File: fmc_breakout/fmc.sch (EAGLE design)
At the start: 1 part

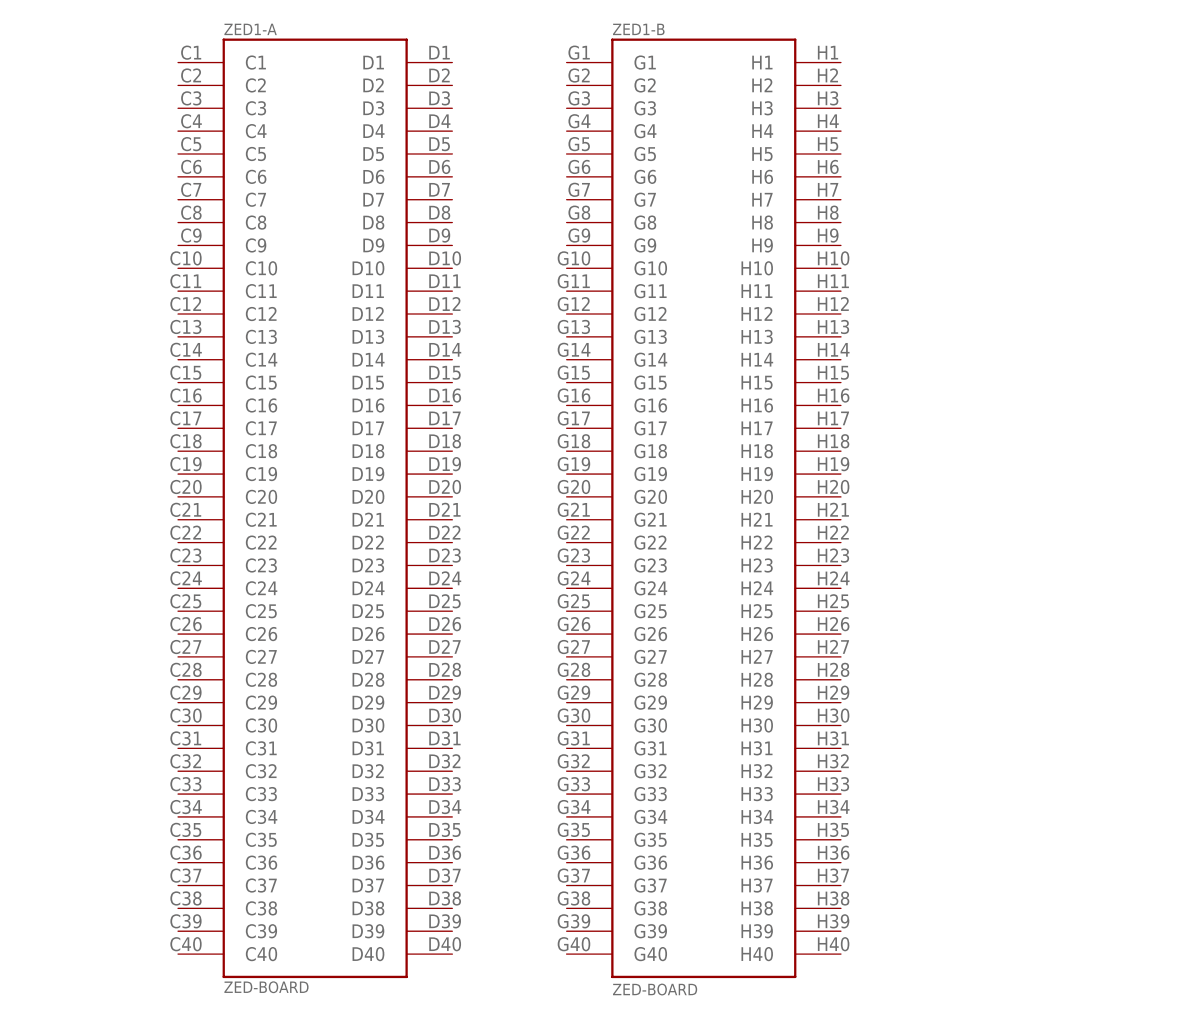
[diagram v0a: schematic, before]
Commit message: started FMC breakout
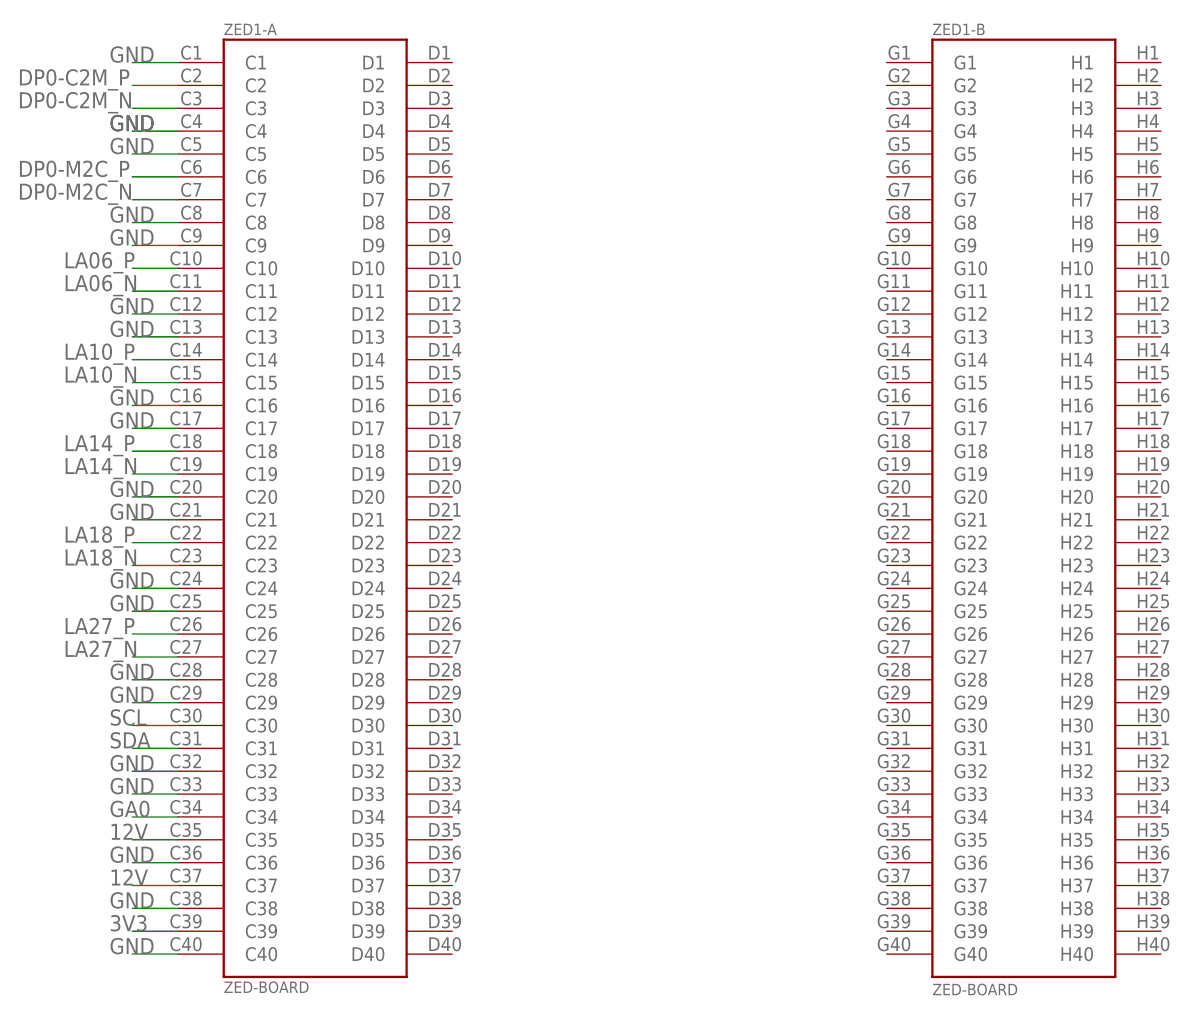
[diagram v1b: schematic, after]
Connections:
- new net 12V: ZED1-A.C35, ZED1-A.C37
- new net 3V3: ZED1-A.C39
- new net DP0-C2M_N: ZED1-A.C3
- new net DP0-C2M_P: ZED1-A.C2
- new net DP0-M2C_N: ZED1-A.C7
- new net DP0-M2C_P: ZED1-A.C6
- new net GA0: ZED1-A.C34
- new net GND: ZED1-A.C1, ZED1-A.C12, ZED1-A.C13, ZED1-A.C16, ZED1-A.C17, ZED1-A.C20, ZED1-A.C21, ZED1-A.C24, ZED1-A.C25, ZED1-A.C28, ZED1-A.C29, ZED1-A.C32, ZED1-A.C33, ZED1-A.C36, ZED1-A.C38, ZED1-A.C4, ZED1-A.C40, ZED1-A.C5, ZED1-A.C8, ZED1-A.C9
- new net LA06_N: ZED1-A.C11
- new net LA06_P: ZED1-A.C10
- new net LA10_N: ZED1-A.C15
- new net LA10_P: ZED1-A.C14
- new net LA14_N: ZED1-A.C19
- new net LA14_P: ZED1-A.C18
- new net LA18_N: ZED1-A.C23
- new net LA18_P: ZED1-A.C22
- new net LA27_N: ZED1-A.C27
- new net LA27_P: ZED1-A.C26
- new net SCL: ZED1-A.C30
- new net SDA: ZED1-A.C31
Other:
- moved on the sheet: ZED1-B

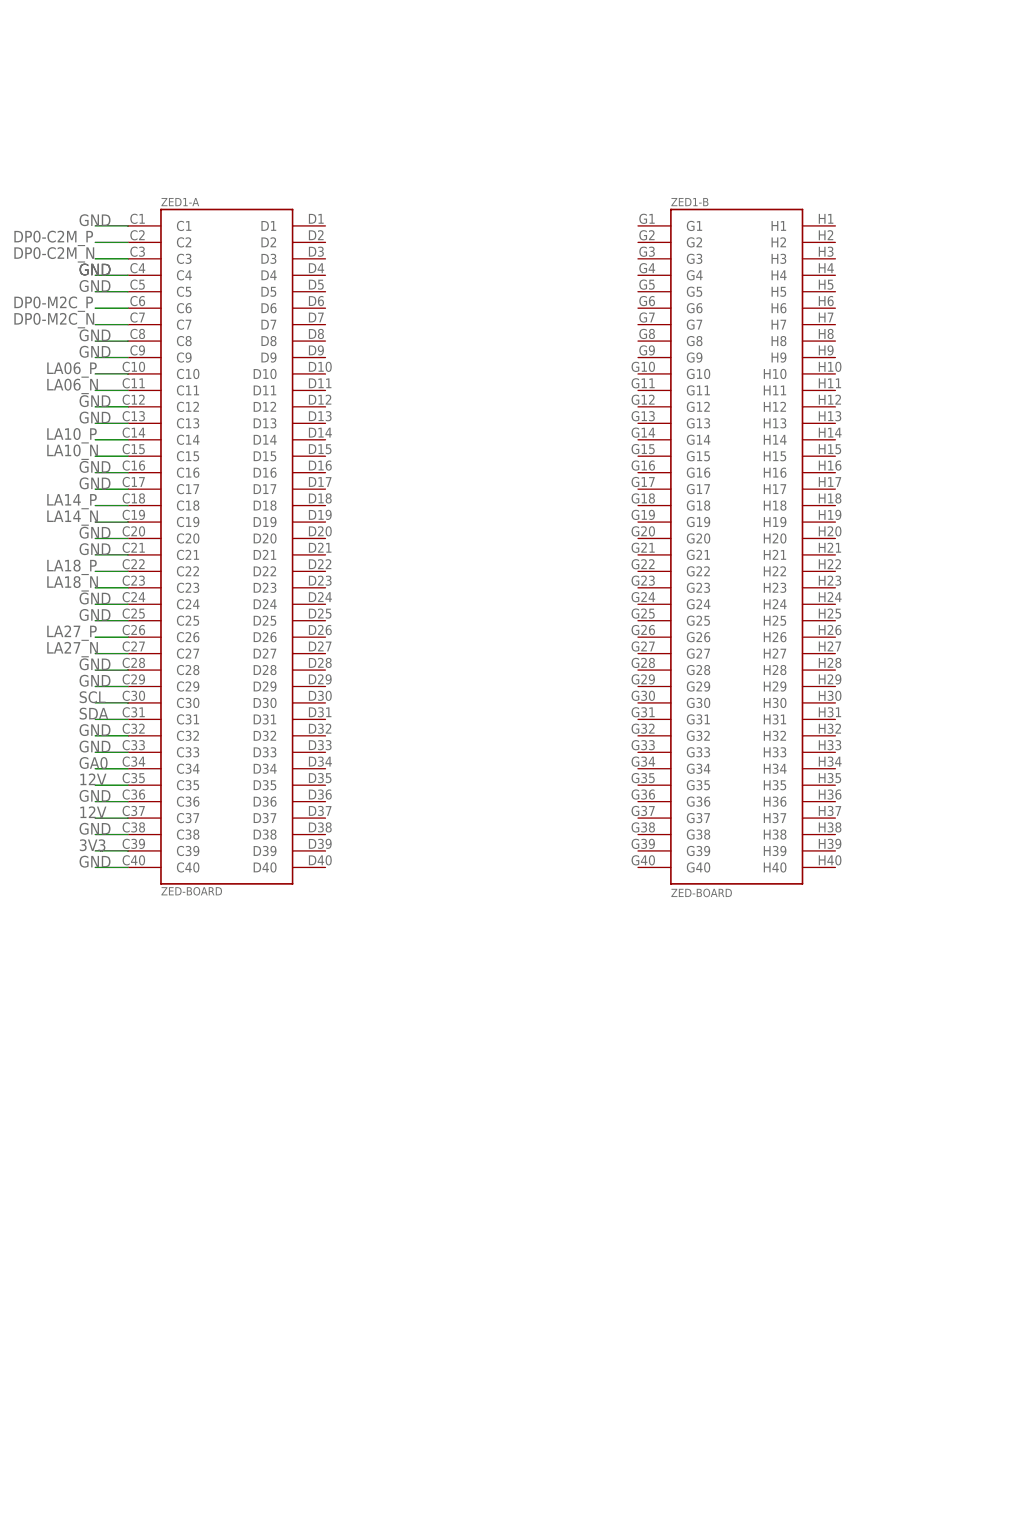
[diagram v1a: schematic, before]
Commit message: FMC bus map
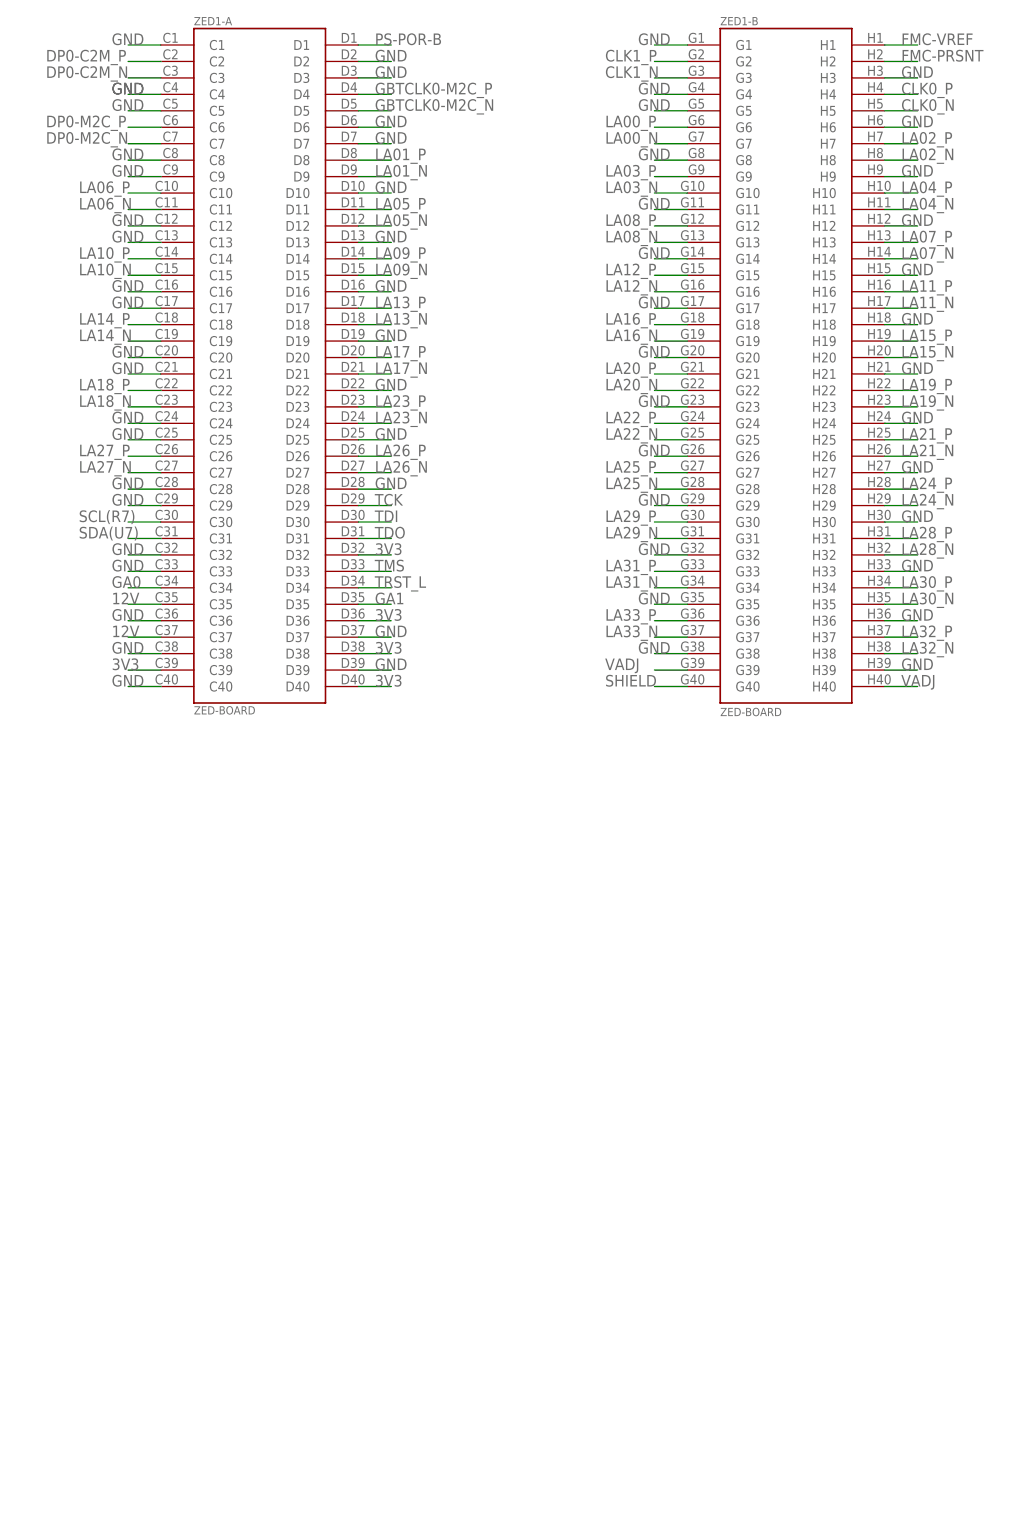
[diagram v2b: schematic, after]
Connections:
- net SCL renamed SCL(R7)
- net SDA renamed SDA(U7)
- new net CLK0_N: ZED1-B.H5
- new net CLK0_P: ZED1-B.H4
- new net CLK1_N: ZED1-B.G3
- new net CLK1_P: ZED1-B.G2
- new net FMC-PRSNT: ZED1-B.H2
- new net FMC-VREF: ZED1-B.H1
- new net GA1: ZED1-A.D35
- new net GBTCLK0-M2C_N: ZED1-A.D5
- new net GBTCLK0-M2C_P: ZED1-A.D4
- new net LA00_N: ZED1-B.G7
- new net LA00_P: ZED1-B.G6
- new net LA01_N: ZED1-A.D9
- new net LA01_P: ZED1-A.D8
- new net LA02_N: ZED1-B.H8
- new net LA02_P: ZED1-B.H7
- new net LA03_N: ZED1-B.G10
- new net LA03_P: ZED1-B.G9
- new net LA04_N: ZED1-B.H11
- new net LA04_P: ZED1-B.H10
- new net LA05_N: ZED1-A.D12
- new net LA05_P: ZED1-A.D11
- new net LA07_N: ZED1-B.H14
- new net LA07_P: ZED1-B.H13
- new net LA08_N: ZED1-B.G13
- new net LA08_P: ZED1-B.G12
- new net LA09_N: ZED1-A.D15
- new net LA09_P: ZED1-A.D14
- new net LA11_N: ZED1-B.H17
- new net LA11_P: ZED1-B.H16
- new net LA12_N: ZED1-B.G16
- new net LA12_P: ZED1-B.G15
- new net LA13_N: ZED1-A.D18
- new net LA13_P: ZED1-A.D17
- new net LA15_N: ZED1-B.H20
- new net LA15_P: ZED1-B.H19
- new net LA16_N: ZED1-B.G19
- new net LA16_P: ZED1-B.G18
- new net LA17_N: ZED1-A.D21
- new net LA17_P: ZED1-A.D20
- new net LA19_N: ZED1-B.H23
- new net LA19_P: ZED1-B.H22
- new net LA20_N: ZED1-B.G22
- new net LA20_P: ZED1-B.G21
- new net LA21_N: ZED1-B.H26
- new net LA21_P: ZED1-B.H25
- new net LA22_N: ZED1-B.G25
- new net LA22_P: ZED1-B.G24
- new net LA23_N: ZED1-A.D24
- new net LA23_P: ZED1-A.D23
- new net LA24_N: ZED1-B.H29
- new net LA24_P: ZED1-B.H28
- new net LA25_N: ZED1-B.G28
- new net LA25_P: ZED1-B.G27
- new net LA26_N: ZED1-A.D27
- new net LA26_P: ZED1-A.D26
- new net LA28_N: ZED1-B.H32
- new net LA28_P: ZED1-B.H31
- new net LA29_N: ZED1-B.G31
- new net LA29_P: ZED1-B.G30
- new net LA30_N: ZED1-B.H35
- new net LA30_P: ZED1-B.H34
- new net LA31_N: ZED1-B.G34
- new net LA31_P: ZED1-B.G33
- new net LA32_N: ZED1-B.H38
- new net LA32_P: ZED1-B.H37
- new net LA33_N: ZED1-B.G37
- new net LA33_P: ZED1-B.G36
- new net PS-POR-B: ZED1-A.D1
- new net SHIELD: ZED1-B.G40
- new net TCK: ZED1-A.D29
- new net TDI: ZED1-A.D30
- new net TDO: ZED1-A.D31
- new net TMS: ZED1-A.D33
- new net TRST_L: ZED1-A.D34
- new net VADJ: ZED1-B.G39, ZED1-B.H40
- net 3V3: now also ZED1-A.D32, ZED1-A.D36, ZED1-A.D38, ZED1-A.D40
- net GND: now also ZED1-A.D10, ZED1-A.D13, ZED1-A.D16, ZED1-A.D19, ZED1-A.D2, ZED1-A.D22, ZED1-A.D25, ZED1-A.D28, ZED1-A.D3, ZED1-A.D37, ZED1-A.D39, ZED1-A.D6, ZED1-A.D7, ZED1-B.G1, ZED1-B.G11, ZED1-B.G14, ZED1-B.G17, ZED1-B.G20, ZED1-B.G23, ZED1-B.G26, ZED1-B.G29, ZED1-B.G32, ZED1-B.G35, ZED1-B.G38, ZED1-B.G4, ZED1-B.G5, ZED1-B.G8, ZED1-B.H12, ZED1-B.H15, ZED1-B.H18, ZED1-B.H21, ZED1-B.H24, ZED1-B.H27, ZED1-B.H3, ZED1-B.H30, ZED1-B.H33, ZED1-B.H36, ZED1-B.H39, ZED1-B.H6, ZED1-B.H9
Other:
- moved on the sheet: ZED1-A, ZED1-B

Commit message: FMC bus pins mapped to FPGA bank locations
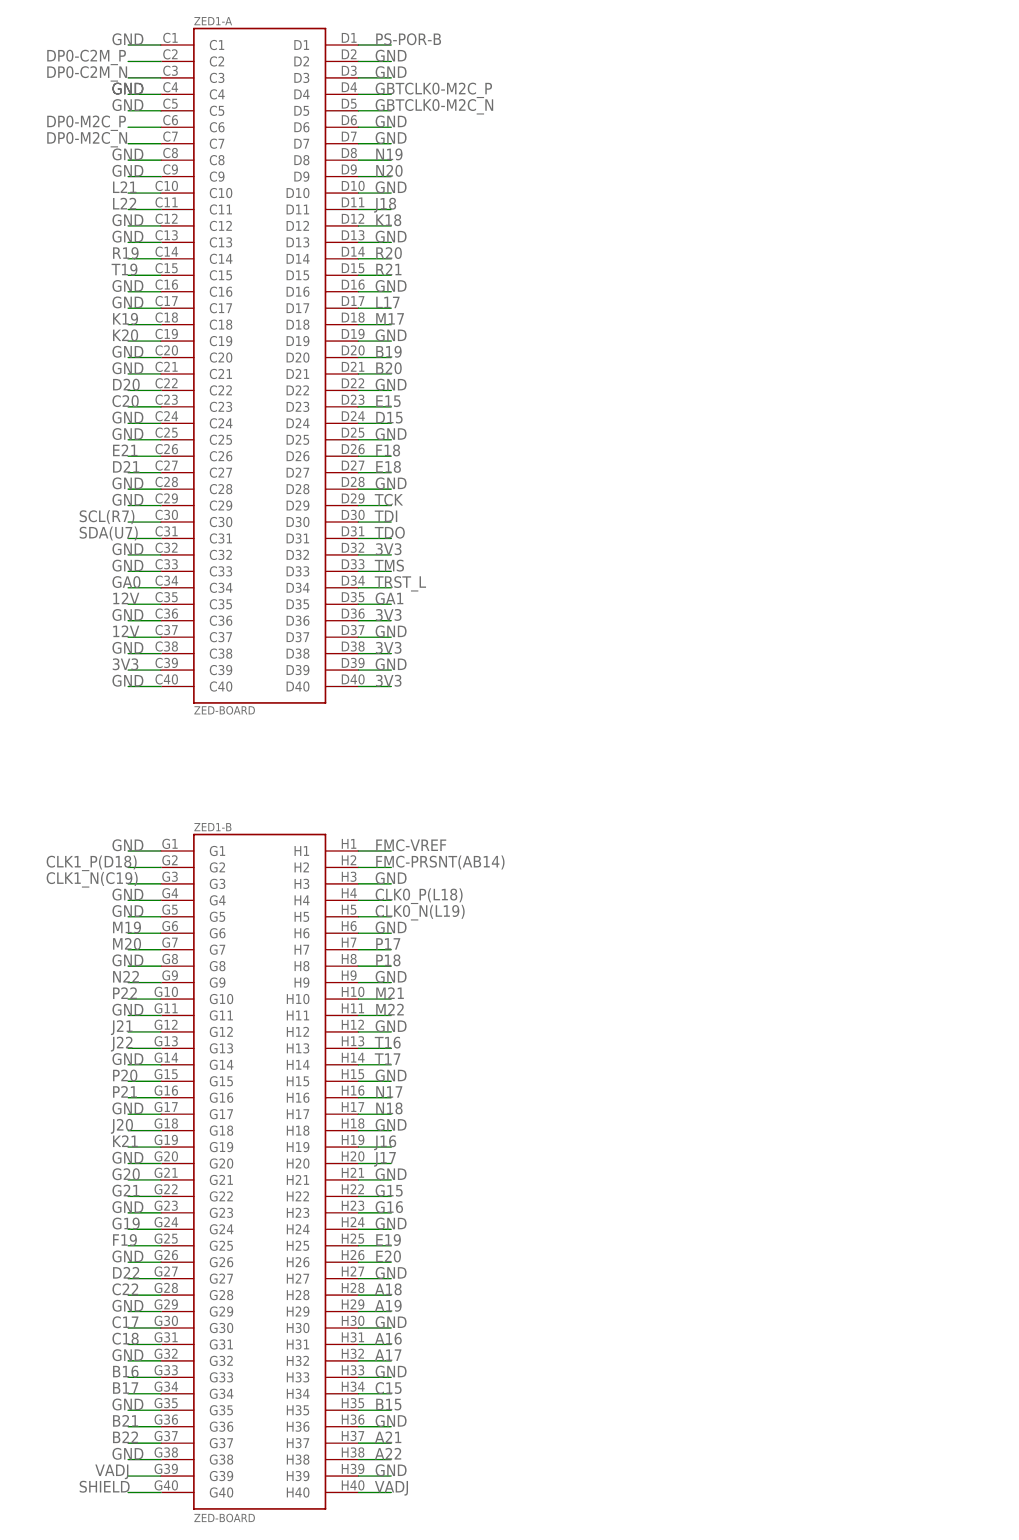
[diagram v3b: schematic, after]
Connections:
- net CLK0_N renamed CLK0_N(L19)
- net CLK0_P renamed CLK0_P(L18)
- net CLK1_N renamed CLK1_N(C19)
- net CLK1_P renamed CLK1_P(D18)
- net FMC-PRSNT renamed FMC-PRSNT(AB14)
- net LA00_N renamed M20
- net LA00_P renamed M19
- net LA01_N renamed N20
- net LA01_P renamed N19
- net LA02_N renamed P18
- net LA02_P renamed P17
- net LA03_N renamed P22
- net LA03_P renamed N22
- net LA04_N renamed M22
- net LA04_P renamed M21
- net LA05_N renamed K18
- net LA05_P renamed J18
- net LA06_N renamed L22
- net LA06_P renamed L21
- net LA07_N renamed T17
- net LA07_P renamed T16
- net LA08_N renamed J22
- net LA08_P renamed J21
- net LA09_N renamed R21
- net LA09_P renamed R20
- net LA10_N renamed T19
- net LA10_P renamed R19
- net LA11_N renamed N18
- net LA11_P renamed N17
- net LA12_N renamed P21
- net LA12_P renamed P20
- net LA13_N renamed M17
- net LA13_P renamed L17
- net LA14_N renamed K20
- net LA14_P renamed K19
- net LA15_N renamed J17
- net LA15_P renamed J16
- net LA16_N renamed K21
- net LA16_P renamed J20
- net LA17_N renamed B20
- net LA17_P renamed B19
- net LA18_N renamed C20
- net LA18_P renamed D20
- net LA19_N renamed G16
- net LA19_P renamed G15
- net LA20_N renamed G21
- net LA20_P renamed G20
- net LA21_N renamed E20
- net LA21_P renamed E19
- net LA22_N renamed F19
- net LA22_P renamed G19
- net LA23_N renamed D15
- net LA23_P renamed E15
- net LA24_N renamed A19
- net LA24_P renamed A18
- net LA25_N renamed C22
- net LA25_P renamed D22
- net LA26_N renamed E18
- net LA26_P renamed F18
- net LA27_N renamed D21
- net LA27_P renamed E21
- net LA28_N renamed A17
- net LA28_P renamed A16
- net LA29_N renamed C18
- net LA29_P renamed C17
- net LA30_N renamed B15
- net LA30_P renamed C15
- net LA31_N renamed B17
- net LA31_P renamed B16
- net LA32_N renamed A22
- net LA32_P renamed A21
- net LA33_N renamed B22
- net LA33_P renamed B21
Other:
- moved on the sheet: ZED1-B
